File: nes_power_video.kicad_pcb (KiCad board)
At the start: 2 copper layers, 59.9 x 59.7 mm, 22 parts, among them J2 Audio, J3 Video, J4 Conn_01x05, J5 RGB conn feed, Q1 2SA1015, U1 TPS2553DBV

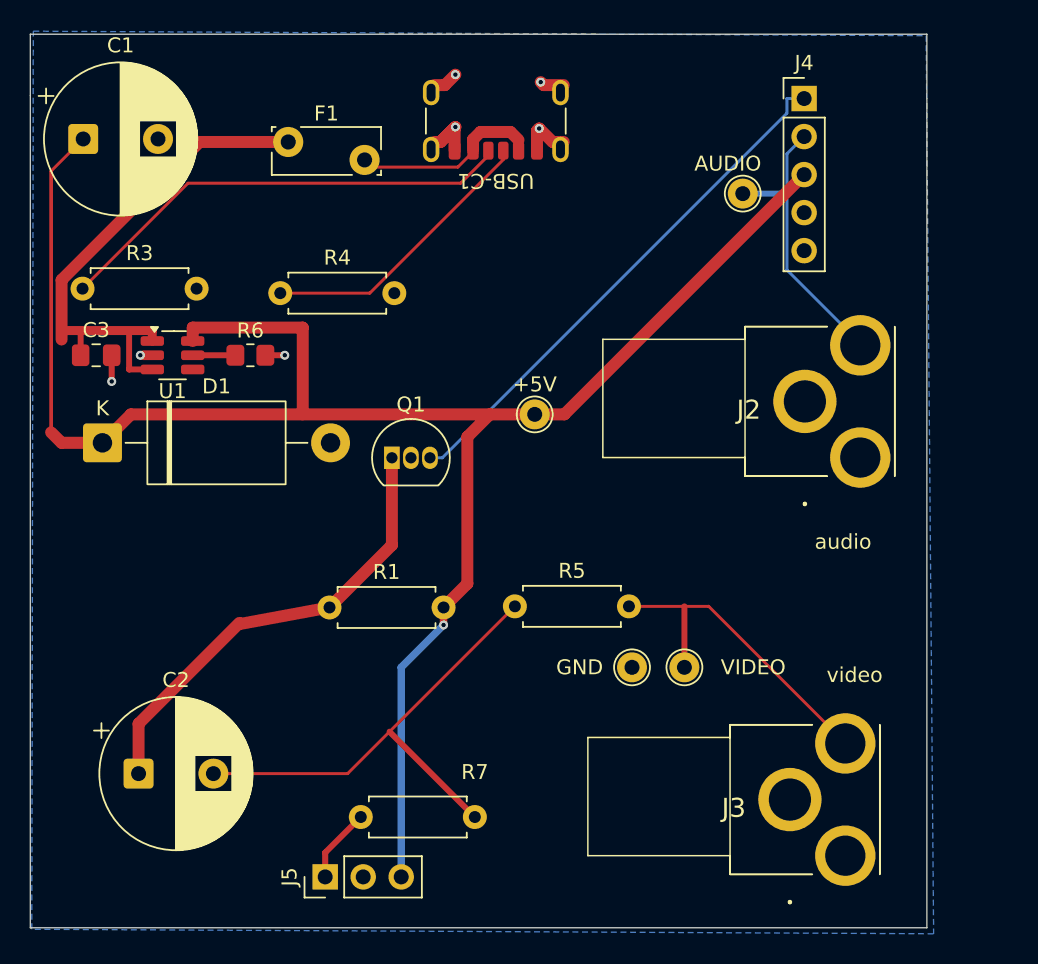
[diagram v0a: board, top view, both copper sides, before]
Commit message: v2 design fixes: R1 to 220R, add R2 base resistor, silkscreen values
R1 300R -> 220R. At the assumed ~1.3V base, 300-330R supplies only ~6.2mA at
peak white against the ~6.7mA the 150R load (R5 75R + TV 75R) needs, so the
follower clips on bright content. 220R gives ~9.3mA.

Add R2, 330R in series between J4 pin 1 and Q1's base, mirroring the 330R
Nintendo places in the same position. Negligible against Q1's ~21k base input
impedance; limits fault current into the base-emitter junction, whose reverse
rating is only 5V. Netlist verified: Net-(Q1-E) is unchanged and 16 of 17
existing nets are byte-identical.

Print all resistor and capacitor values on the silkscreen. R1/R3/R4/R5/R7
share one axial footprint across four values with nothing to tell them apart,
which produced three separate wrong-resistor errors in R1 on the prototype.

C2 to 470uF in the BOM to match what the design needs: into the 150R load,
100uF gives tau=15ms against the 16.7ms field period. F1 value field carried
the library name instead of a rating.

README: document why the board exists (the RF modulator cooks its own
electrolytics - three for three on the bench), the video input biasing and the
1k pulldown the NES mainboard supplies, KSA1015 sourcing for the obsolete
2SA1015, and the lead-trimming requirement for bottom-side clearance.

ERC 0 violations. DRC 2 pre-existing J2/J3 silk warnings, 0 unconnected.

Co-Authored-By: Claude Opus 5 <noreply@anthropic.com>
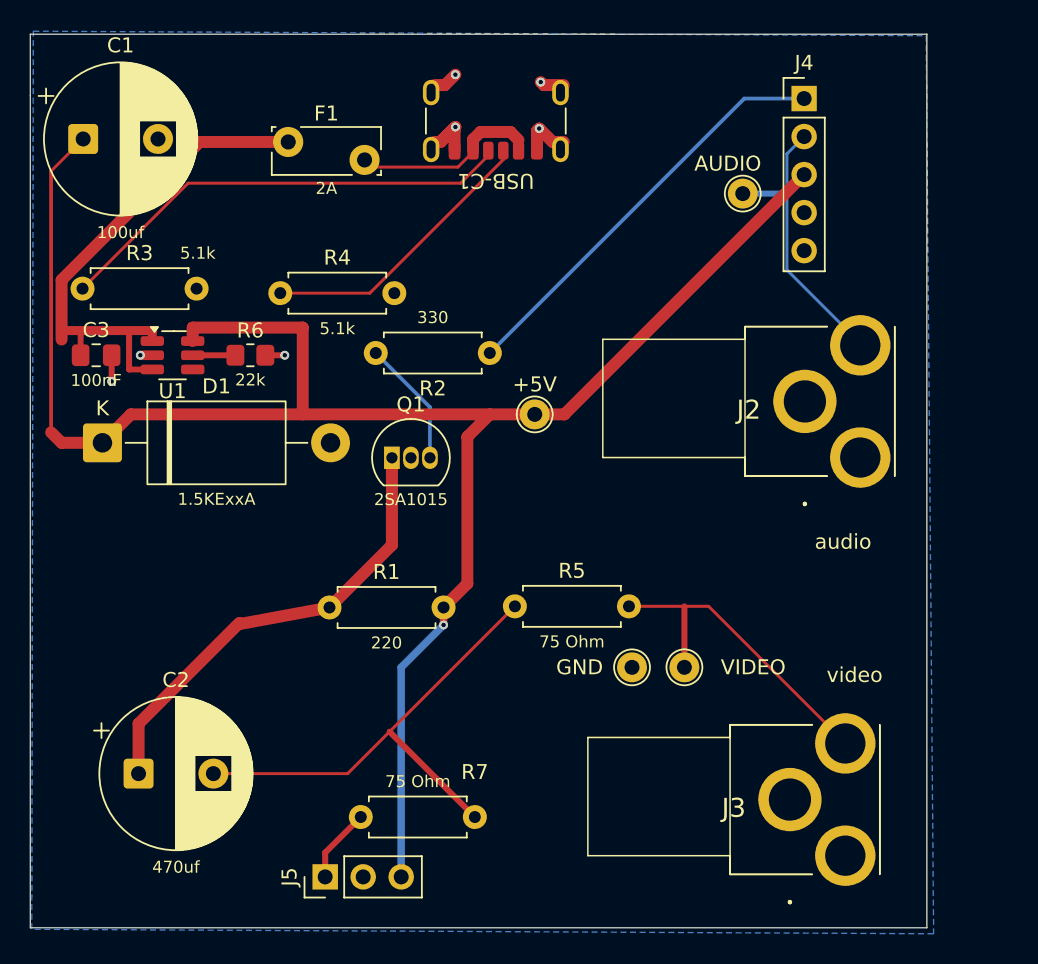
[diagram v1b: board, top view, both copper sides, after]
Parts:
- added R2: 330, Resistor_THT:R_Axial_DIN0207_L6.3mm_D2.5mm_P7.62mm_Horizontal, F.Cu at (49.0, 39.0)
- C2: value 100uf -> 470uf
- F1: value Polyfuse_Small -> 2A
- R1: value 300 -> 220
- R7: footprint R_Axial_DIN0207_L6.3mm_D2.5mm_P7.62mm_Horizontal -> Resistor_THT:R_Axial_DIN0207_L6.3mm_D2.5mm_P7.62mm_Horizontal
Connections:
- Q1 pad 3: Net-(J4-Pin_1) -> Net-(Q1-B)
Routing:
- net Net-(Q1-B): track 0.00 -> 8.50 mm
- net Net-(J4-Pin_1): track 35.5 -> 28.0 mm

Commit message: Fix zone fill and stale track left by the RCA jack rotation
Rotating J2/J3 180 degrees to face the barrels off the board edge moved
their pads, and the reroute left two problems that check_nets.py cannot
see, because both are copper geometry rather than netlist membership:

- The GND pour was never refilled, so all ten /AUDIO_OUT segments on
  B.Cu sat inside solid ground copper - an audio-to-GND short. Eight
  were geometrically inside the filled polygon; KiCad DRC reported
  0.000 mm clearance on all ten.
- A 0.24 mm /AUDIO_OUT stub was left behind at (73.750, 38.484), which
  is J2's pre-rotation TIP pad.

Deleted the stub and refilled the zone. DRC 17 -> 7 violations, with
every remaining one cosmetic: silkscreen clipped at the board edge and
the TP1/J3 courtyard margin, both caused by the barrels overhanging the
edge as intended.

README: R1 has been 220 ohm since 548343f, but the "one output at a
time" section still said 330 ohm. Replaced the hand-calculated clipping
estimate with ngspice results - at 2 Vpp on the tap with both outputs
terminated, 330 ohm clips positive peaks by 33% and 220 ohm by 11%;
a single loaded output is clean and symmetric.

The 2026-08-26 fab package is unaffected: its copper and outline gerbers
are byte-identical to HEAD and all 49 drill hits match, and refilling
HEAD's zones changes nothing.

Co-Authored-By: Claude Opus 5 <noreply@anthropic.com>
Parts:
- turned J2 to 180 degrees
- turned J3 to 180 degrees
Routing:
- net /VIDEO_OUT: track 22.2 -> 34.8 mm
- net /AUDIO_OUT: track 19.4 -> 31.8 mm

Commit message: Give every part a manufacturer, MPN, datasheet and supplier link
The TPS2553 verification from the last session only ever landed in a
gitignored datasheet PDF: the schematic still carried U1 as a bare
"TPS2553DBV" with an empty Datasheet field, and the exported fab BOM had
no manufacturer at all. That is the gap that let the EN-polarity question
stay open long enough to nearly buy the wrong part.

Every component instance now carries Manufacturer / MPN / LCSC /
Supplier Link / Datasheet fields, mirrored into BOM.csv as columns.
Jellybean passives get a Spec field (tolerance, rating, package) rather
than an invented part number - there is no MPN for a 220R axial resistor.

Specifics:
- U1: TPS2553DBVR, LCSC C55266, TI SLVS841F datasheet
- C3 / R6: pinned to JLCPCB basic parts C49678 and C17560; R6 keeps 1%
  because it sets the eFuse current limit
- Q1: datasheet was a dead datasheetcatalog.org link (404). Now onsemi
  KSA1015, which is what the BOM already told you to buy
- J2 / J3: datasheet moved off a Mouser link that no longer serves the
  PDF, onto Switchcraft's own drawing. Vendor field names normalised to
  Manufacturer / MPN
- USB-C1: datasheet was the generic USB-IF Type-C spec zip; now the GCT
  USB4970 drawing
- J2, J3 and J4 were missing from BOM.csv entirely
- D1's value read "1.5KExxA" - the KiCad symbol name, not a part you can
  order - in the schematic and on the silkscreen. Now 1.5KE6.8A, matching
  what the BOM has always said

Project-local symbol libraries carry the same fields so future
placements inherit them, and the cached lib_symbols were synced to match
(an unsynced cache raises lib_symbol_mismatch in ERC).

Verified: ERC 0 violations, check_nets.py all invariants pass, 14 nets
identical sch/pcb, DRC violation set unchanged from HEAD (7 pre-existing,
all J2/J3/TP1 silkscreen and courtyard from the jack rotation).

Co-Authored-By: Claude Opus 5 <noreply@anthropic.com>
Claude-Session: https://claude.ai/code/session_01SFPsiQ6ZtUgKSkh2NG4xCg
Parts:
- D1: value 1.5KExxA -> 1.5KE6.8A
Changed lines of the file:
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@@
 			)
 		)
-		(property "Value" "1.5KExxA"
+		(property "Value" "1.5KE6.8A"
 			(at 7.62 3.77 0)
 			(layer "F.SilkS")

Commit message: Fix Q1 silkscreen, USB-C footprint variant, and document F1's borrowed land pattern
Q1: the silkscreen printed 2SA1015, a discontinued part. It now prints
KSA1015, the onsemi part the BOM tells you to buy - same E-C-B pinout,
still in production. Schematic value and BOM value follow.

USB-C1: this was half a real bug. KiCad has no USB4970 footprint, but
GCT's USB4970 drawing specifies exactly the USB4125 land pattern - pad
centres 1.00/3.04/5.50 mm, widths 0.70/0.76/0.80 x 1.20 mm, shell holes
8.64 x 3.80 mm apart at 1.10 x 1.70 mm with 0.60 x 1.20 mm slots - which
is pad-for-pad what Connector_USB:USB_C_Receptacle_GCT_USB4125-xx-x
carries. So the copper was always right. What was wrong is the variant:
we had -0190, the 1.90 mm shell stake, while USB4970-00-A is the blank
suffix, 1.00 mm stake (GCT ordering grid). Switched to the plain
footprint, whose geometry is byte-identical apart from the name, descr
and 3D model, so not one pad moved. USB-C1's fab-layer value read
USB_C_Receptacle_PowerOnly_6P, a KiCad symbol name; now USB4970-00-A.

F1: no KiCad footprint exists for the Littelfuse RHEF series, so F1
borrows Fuse:Fuse_Bourns_MF-RG300 - pads at (0,0) and (5.1,1.2),
5.24 mm centre-to-centre, 1.01 mm drills. Per the RHEF datasheet the
RHEF200 has 0.51 mm (24 AWG) leads at 5.05 +/-0.75 mm spacing, so it
fits with room to spare. But the Bourns device is rated 3.0 A/5.1 A
against the RHEF200's 2.0 A/3.8 A, and the silkscreen outline is the
Bourns body - recorded as a Footprint Note field on F1, in BOM.csv and
in the README so nobody reads that outline as a clearance boundary.
Drawing a true RHEF200 footprint would move pad 2 by ~1.2 mm and force a
re-route, so it is a v3 change rather than a patch.

Verified: ERC 0 violations, check_nets.py all invariants pass, DRC
violation set identical to the previous commit, and the PCB diff is five
lines with no pad, track, via or zone touched.

Co-Authored-By: Claude Opus 5 <noreply@anthropic.com>
Claude-Session: https://claud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
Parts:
- Q1: value 2SA1015 -> KSA1015
- USB-C1: value USB_C_Receptacle_PowerOnly_6P -> USB4970-00-A; footprint Connector_USB:USB_C_Receptacle_GCT_USB4125-xx-x-0190_6P_TopMnt_Horizontal -> Connector_USB:USB_C_Receptacle_GCT_USB4125-xx-x_6P_TopMnt_Horizontal
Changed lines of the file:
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@@
 		)
 	)
-	(footprint "Connector_USB:USB_C_Receptacle_GCT_USB4125-xx-x-0190_6P_TopMnt_Horizontal"
+	(footprint "Connector_USB:USB_C_Receptacle_GCT_USB4125-xx-x_6P_TopMnt_Horizontal"
 		(layer "F.Cu")
 		(at 49.4 22.4 180)
-		(descr "USB Type C Receptacle, GCT, power-only, 6P, top mounted, horizontal, 3A, 1.9mm stake: https://gct.co/files/drawings/usb4125.pdf")
+		(descr "USB Type C Receptacle, GCT, power-only, 6P, top mounted, horizontal, 3A, 1mm stake: https://gct.co/files/drawings/usb4125.pdf")
 		(tags "USB C Type-C receptacle power-only charging-only 6P 6C right angled")
 		(property "Reference" "USB-C1"
@@
 			)
 		)
-		(property "Value" "USB_C_Receptacle_PowerOnly_6P"
+		(property "Value" "USB4970-00-A"
 			(at 0 4.725 180)
 			(unlocked yes)
@@
 		)
 		(embedded_fonts no)
-		(model "${KICAD10_3DMODEL_DIR}/Connector_USB.3dshapes/USB_C_Receptacle_GCT_USB4125-xx-x-0190_6P_TopMnt_Horizontal.step"
+		(model "${KICAD10_3DMODEL_DIR}/Connector_USB.3dshapes/USB_C_Receptacle_GCT_USB4125-xx-x_6P_TopMnt_Horizontal.step"
 			(offset
 				(xyz 0 0 0)
@@
 			)
 		)
-		(property "Value" "2SA1015"
+		(property "Value" "KSA1015"
 			(at 1.27 2.79 0)
 			(layer "F.SilkS")

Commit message: Switch Q1 to the 2SA733: in production, drop-in pinout, better part
Both previous candidates are end of life, so Q1 was specified on borrowed
time either way. The 2SA733 is in current production from UTC, shares the
E-C-B pin order exactly - collector in the middle - so it drops into the
existing TO-92 footprint with no layout change, and it is a better part
for a video buffer than what it replaces:

  fT   190 MHz typ   vs the 2SA1015's 80 MHz
  Cob  2-3 pF
  PC   750 mW (TO-92)
  VCEO -50 V, IC -150 mA, VEBO -5 V   unchanged, so R2 still guards B-E

Rank P is hFE 200-400, matching the ~46 uA base current measured on the
bench at ~9.3 mA emitter, so the bias point does not move and no other
component changes. Buy UTC 2SA733L-P-T92-B from LCSC (C5310429, $0.035):
DigiKey's Renesas 2SA733 shows Active with 81k stock but ships from
Rochester at $1.90, the same last-time-buy channel the KSA1015 was stuck
in. Pinout confirmed from UTC's ordering table, not from a drawing.

The README's 2N3906 warning was accurate but read as if the part were
electrically unsuitable, which it is not. Rewritten to say what actually
bites: the 2N3906 is E-B-C against the 2SA733's E-C-B, so it puts BASE in
the middle pin where this board wants COLLECTOR. Rotating it gives C-B-E
and base is still in the middle, so no orientation fixes it - it needs two
leads crossed. On a v3 layout the pin order is free and the 2N3906 becomes
a good choice; on this board it is not.

Schematic keeps the Transistor_BJT:2SA1015 symbol - same pinout family,
and swapping it would only churn the cached lib_symbols.

Verified: ERC 0 violations, check_nets.py all invariants pass, DRC
violation set identical to the previous commit, both new links resolve
(LCSC 200, UTC datasheet 200 application/pdf). Silkscreen now reads
2SA733; no copper touched.

Co-Authored-By: Claude Opus 5 <noreply@anthropic.com>
Claude-Session: https://claude.ai/code/session_01SFPsiQ6ZtUgKSkh2NG4xCg
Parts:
- Q1: value KSA1015 -> 2SA733
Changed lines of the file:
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@@
 			)
 		)
-		(property "Value" "KSA1015"
+		(property "Value" "2SA733"
 			(at 1.27 2.79 0)
 			(layer "F.SilkS")
